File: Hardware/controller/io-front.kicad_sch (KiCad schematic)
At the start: 14 parts

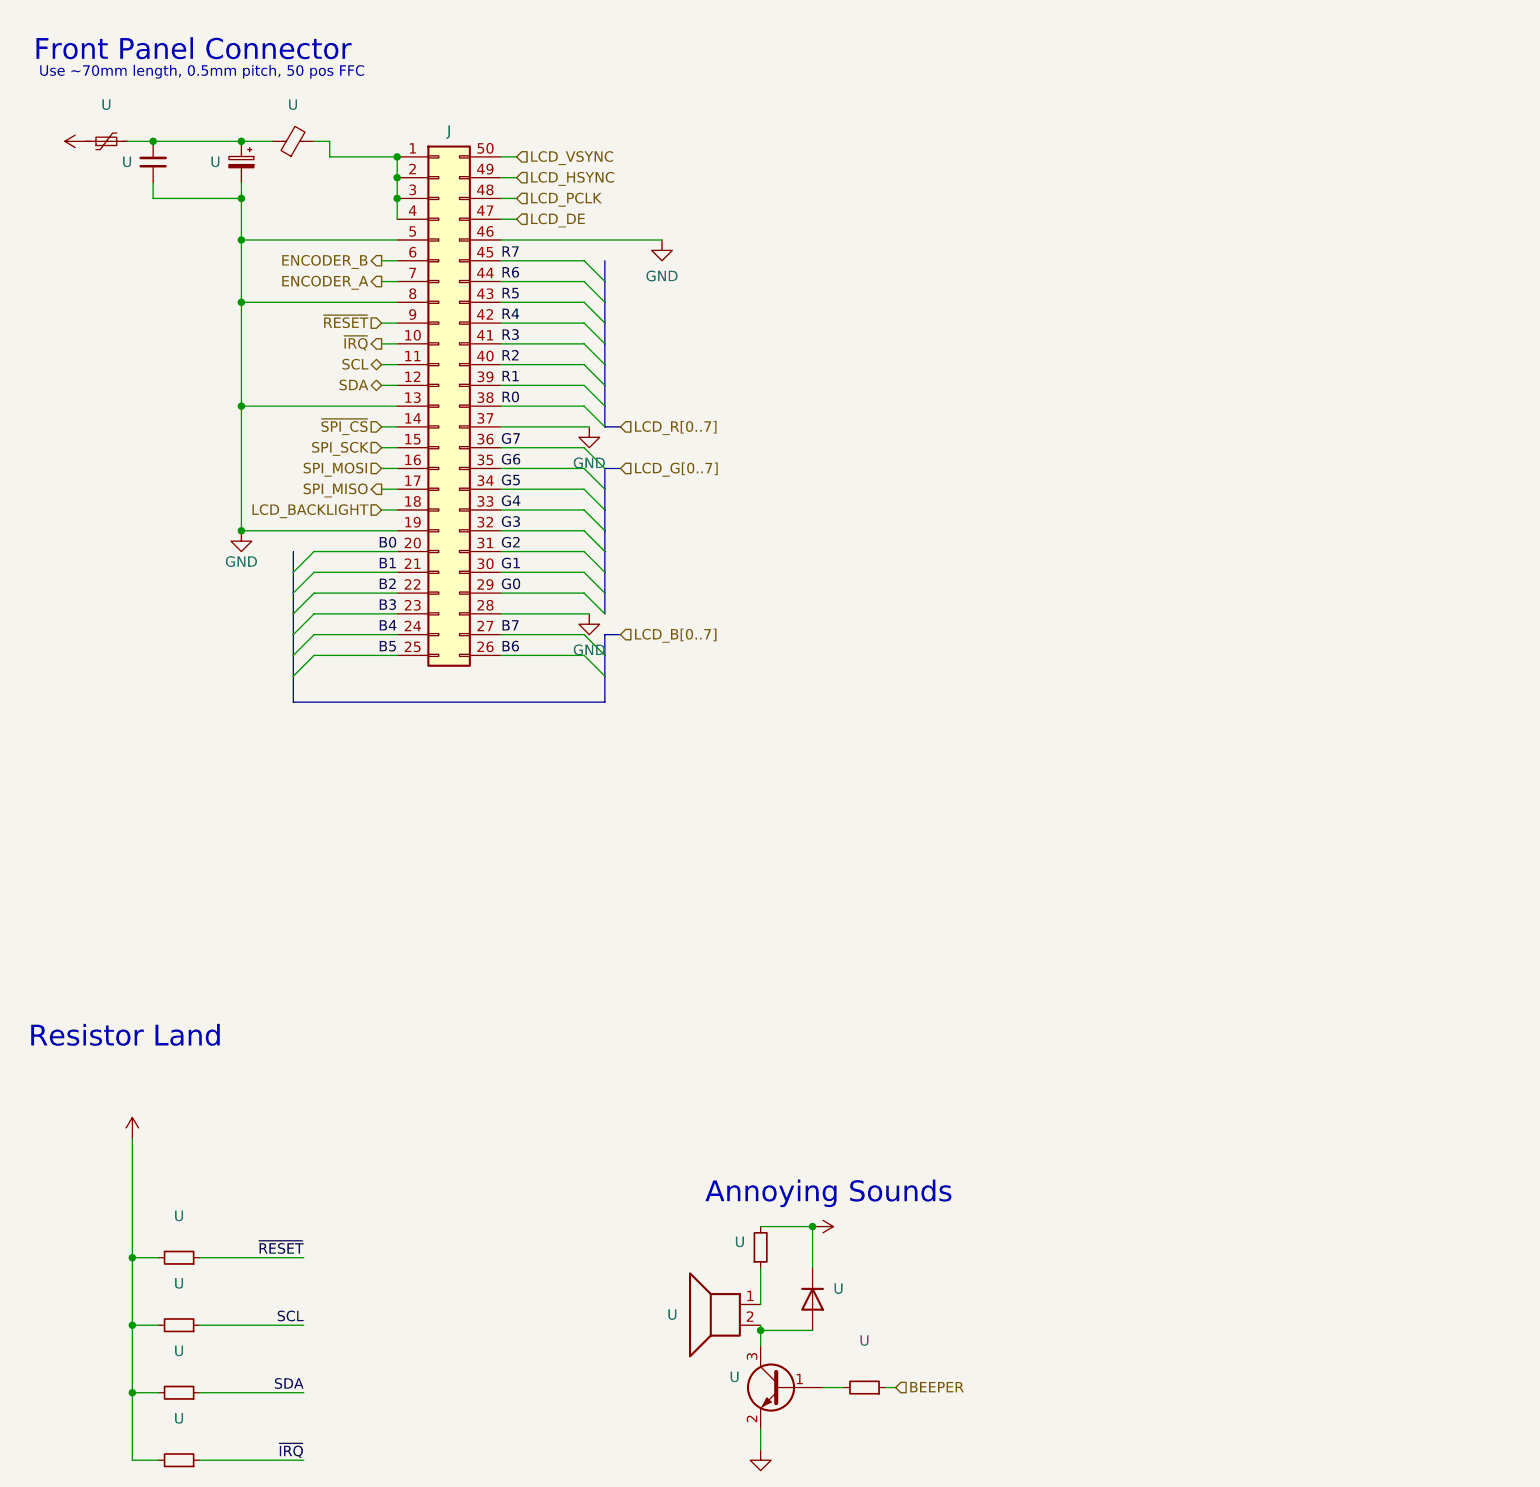
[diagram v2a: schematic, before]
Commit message: Route controller front panel connections
- Routed the connections to the front panel flex connector (the RGB
  interface, SPI + I2C, and various control signals and its fused power
  rail) and the SoM

- Tweaked SoM symbols and footprint

- Added symbols for 4x 2:1 analog switch (SN74CBTLV3257)
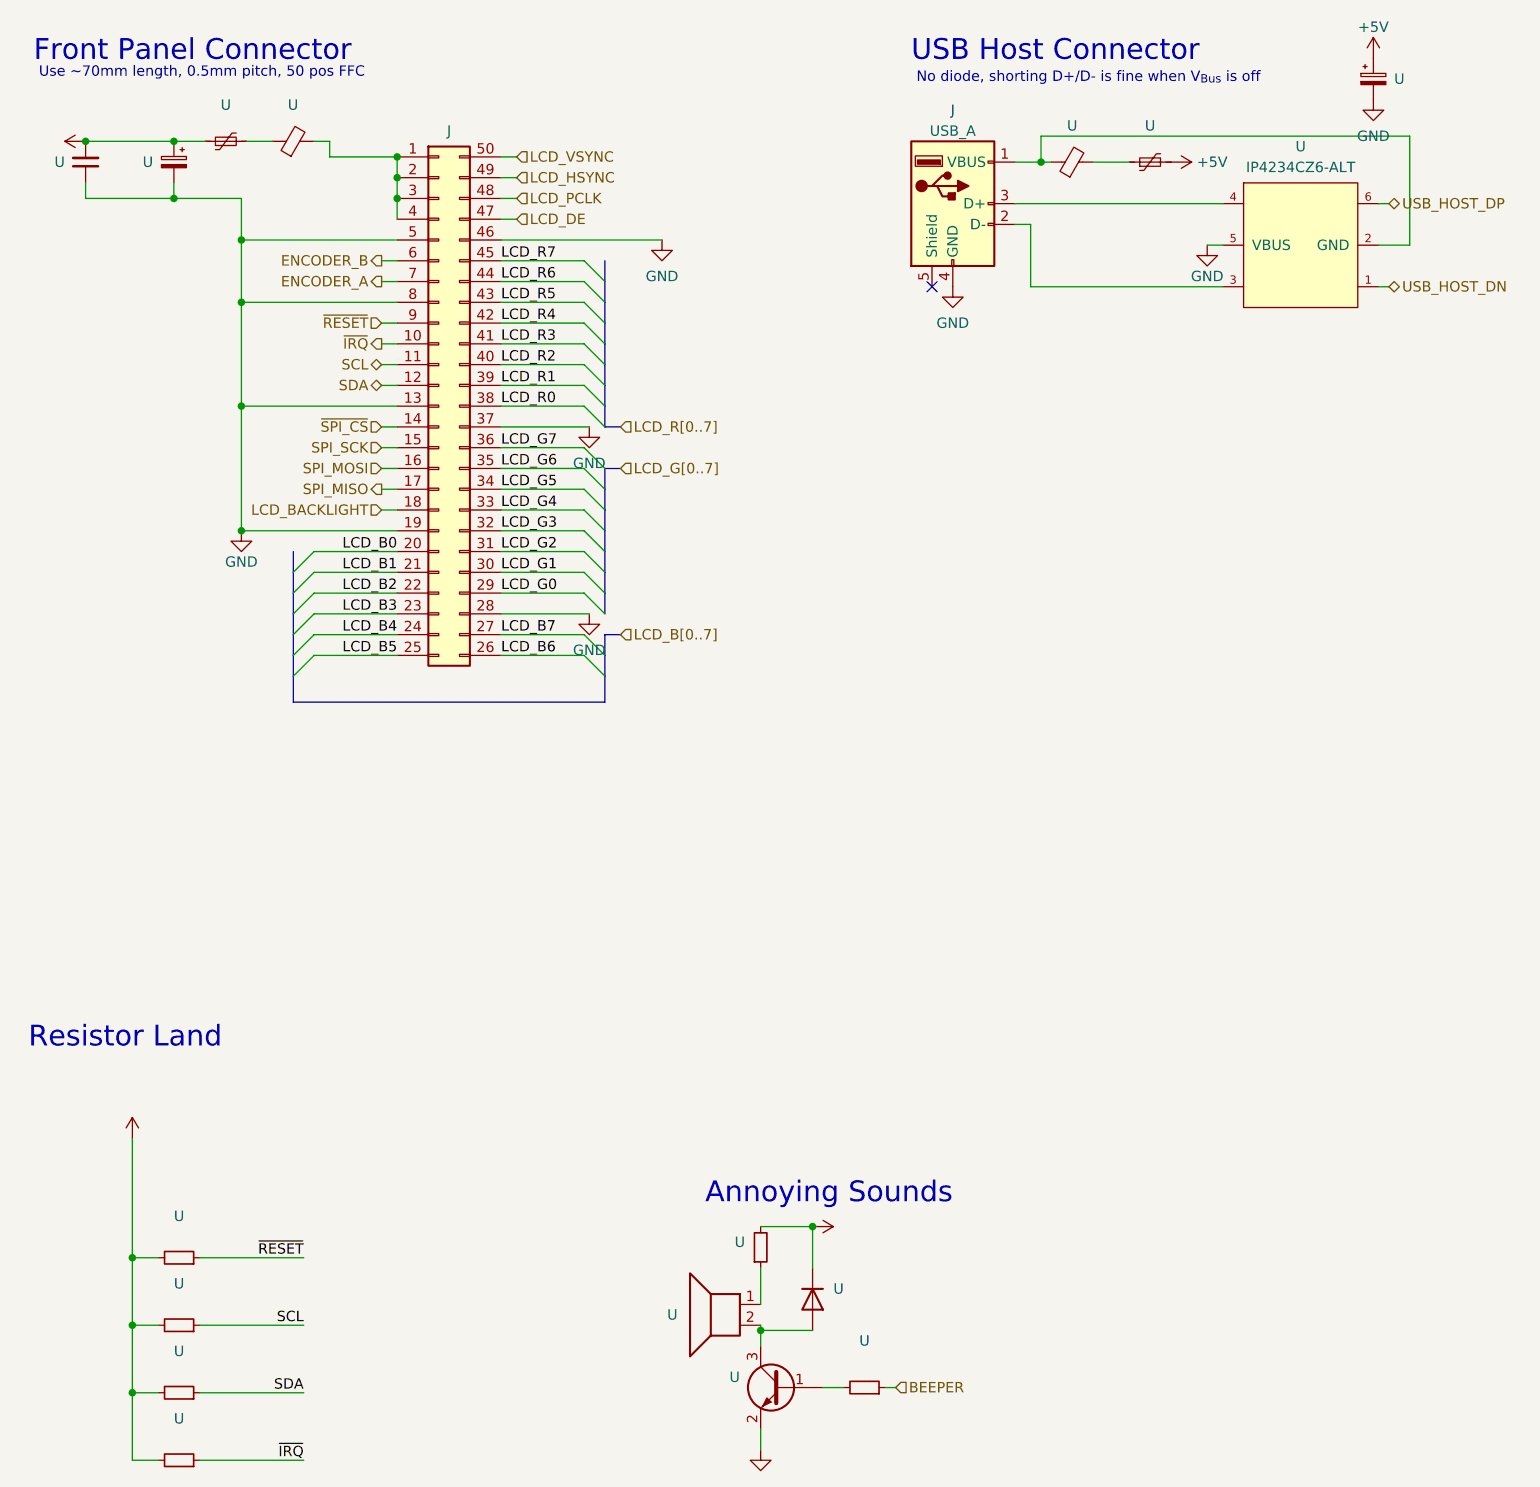
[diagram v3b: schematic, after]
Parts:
- added J: USB_A, symbol Connector:USB_A
- added U: (no value), symbol Device:Polyfuse_Small
- added U: (no value), symbol Device:FerriteBead_Small
- added U: IP4234CZ6-ALT, Package_SO:TSOP-6_1.65x3.05mm_P0.95mm, symbol programmable-load:IP4234CZ6-ALT
- added U: (no value), symbol Device:C_Polarized_Small
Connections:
- net +3V3: now also U.1, U.2
- net GND: now also J.4 (GND), U.2, U.5 (VBUS)
- net at U.1, U.2: no longer U.1, U.2
- net B0 renamed LCD_B0
- net B1 renamed LCD_B1
- net B2 renamed LCD_B2
- net B3 renamed LCD_B3
- net B4 renamed LCD_B4
- net B5 renamed LCD_B5
- net B6 renamed LCD_B6
- net B7 renamed LCD_B7
- net G0 renamed LCD_G0
- net G1 renamed LCD_G1
- net G2 renamed LCD_G2
- net G3 renamed LCD_G3
- net G4 renamed LCD_G4
- net G5 renamed LCD_G5
- net G6 renamed LCD_G6
- net G7 renamed LCD_G7
- net R0 renamed LCD_R0
- net R1 renamed LCD_R1
- net R2 renamed LCD_R2
- net R3 renamed LCD_R3
- net R4 renamed LCD_R4
- net R5 renamed LCD_R5
- net R6 renamed LCD_R6
- net R7 renamed LCD_R7
- new net: U.1, U.2
- new net: J.1 (VBUS), U.1, U.2 (GND)
- new net: J.2 (D-), U.3
- new net: J.3 (D+), U.4
- new net +5V: U.1, U.2
- new net USB_HOST_DN: U.1
- new net USB_HOST_DP: U.6
- no-connect marks 0 -> 1
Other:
- note added: "No diode, shorting D+/D- is fine when V_{Bus} is off"
- note added: "USB Host Connector"
- moved on the sheet: U

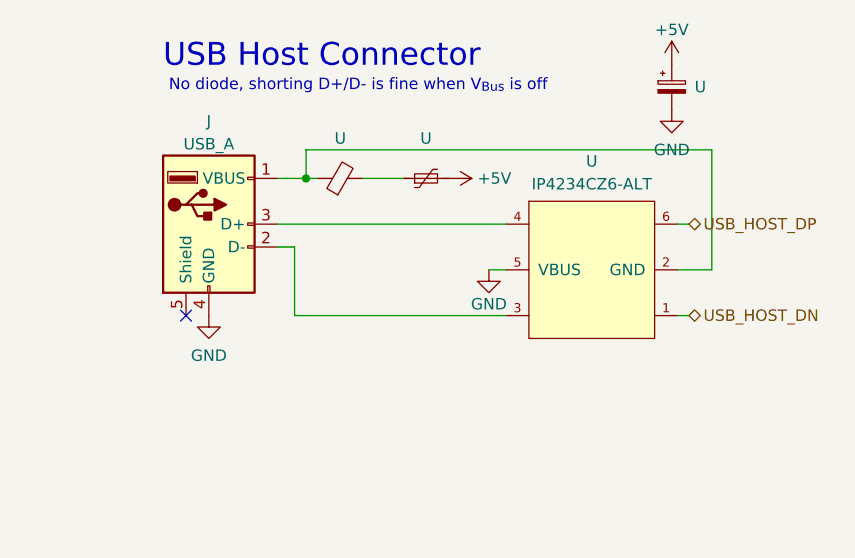
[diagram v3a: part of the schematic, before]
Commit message: More rework of controller
- Updated power section to use a transformer + DC/DC modules, rather
  than a switching AC/DC supply: this should result in fewer bits of
  random noise floating around

- Moved a bunch of stuff around, and changed pinouts slightly of
  external connectors

- Start work on removing dependency on rear IO board

- Minor tweaks to part numbers on front panel board
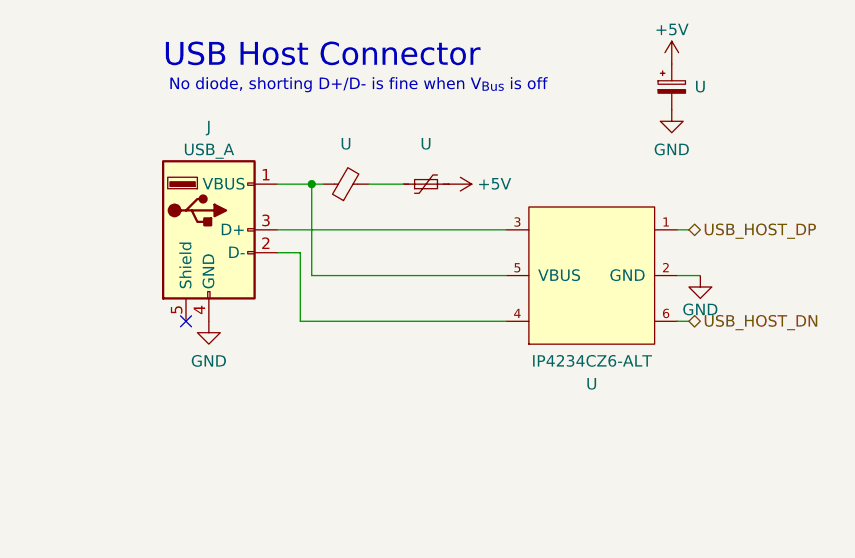
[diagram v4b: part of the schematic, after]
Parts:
- U: MPN EMVA250ADA470MF55G -> APA0606220M035R
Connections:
- net GND: now also U.2 (GND); no longer U.5 (VBUS)
- net USB_HOST_DN: now also U.6; no longer U.1
- net USB_HOST_DP: now also U.1; no longer U.6
- net at J.1 (VBUS), U.1: now also U.5 (VBUS); no longer U.2 (GND)
- net at J.2 (D-): now also U.4; no longer U.3
- net at J.3 (D+): now also U.3; no longer U.4
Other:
- moved on the sheet: J, U

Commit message: Replaced most passives with 0603 size
- This is more compact, and we might as well since this board will be at
  least partially assembled beforehand
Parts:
- U: MPN RMC1/10-103JTP -> (none)
- U: MPN RMC1/10-222JTP -> (none)
- U: MPN RMC1/10-331JTP -> (none)
- U: MPN CL21B104KACNFNC -> (none)
- U: MPn RMC1/10-331JTP -> (none)
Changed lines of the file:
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@@
       (effects (font (size 1.27 1.27)) hide)
     )
-    (property "MPN" "RMC1/10-103JTP" (id 4) (at 37.465 189.865 90)
+    (property "MPN" "" (id 4) (at 37.465 189.865 90)
       (effects (font (size 1.27 1.27)) hide)
     )
@@
       (effects (font (size 1.27 1.27)) hide)
     )
-    (property "MPN" "RMC1/10-103JTP" (id 4) (at 37.465 165.1 90)
+    (property "MPN" "" (id 4) (at 37.465 165.1 90)
       (effects (font (size 1.27 1.27)) hide)
     )
@@
       (effects (font (size 1.27 1.27)) hide)
     )
-    (property "MPN" "RMC1/10-222JTP" (id 4) (at 37.465 181.61 90)
+    (property "MPN" "" (id 4) (at 37.465 181.61 90)
       (effects (font (size 1.27 1.27)) hide)
     )
@@
       (effects (font (size 1.27 1.27)) hide)
     )
-    (property "MPN" "RMC1/10-222JTP" (id 4) (at 37.465 173.355 90)
+    (property "MPN" "" (id 4) (at 37.465 173.355 90)
       (effects (font (size 1.27 1.27)) hide)
     )
@@
       (effects (font (size 1.27 1.27)) hide)
     )
-    (property "MPN" "RMC1/10-331JTP" (id 4) (at 108.585 163.83 0)
+    (property "MPN" "" (id 4) (at 108.585 163.83 0)
       (effects (font (size 1.27 1.27)) hide)
     )
@@
       (effects (font (size 1.27 1.27)) hide)
     )
-    (property "MPN" "CL21B104KACNFNC" (id 4) (at 26.035 31.115 0)
+    (property "MPN" "" (id 4) (at 26.035 31.115 0)
       (effects (font (size 1.27 1.27)) hide)
     )
@@
       (effects (font (size 1.27 1.27)) hide)
     )
-    (property "MPn" "RMC1/10-331JTP" (id 4) (at 121.285 180.975 0)
-      (effects (font (size 1.27 1.27)) hide)
-    )
+    (property "MPn" "" (id 4) (at 121.285 180.975 0)
+      (effects (font (size 1.27 1.27)) hide)
+    )

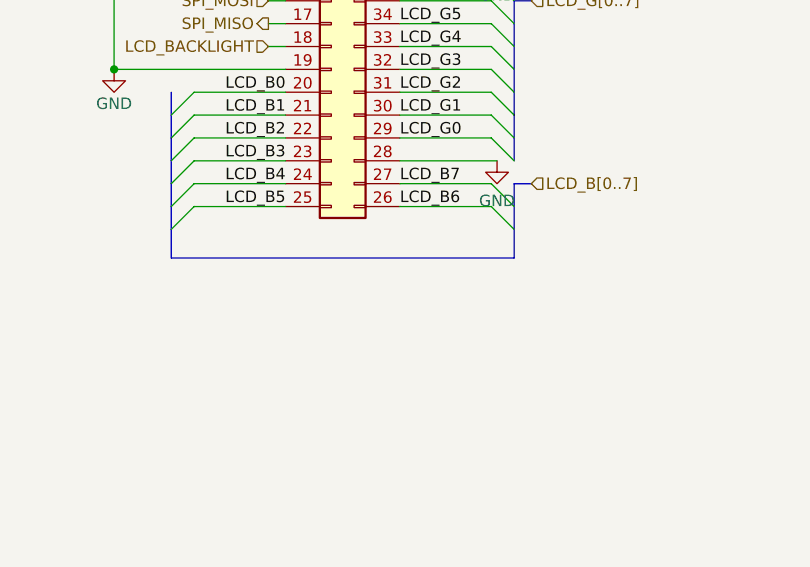
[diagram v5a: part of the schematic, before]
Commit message: Routed Ethernet PHY
- Finished routing the RMII lines to the Ethernet PHY, all of its power
  stuff, and routing its output signals to the Ethernet magjack on the
  side of the board

  This probably needs some revisiting re: the LAN8720 reference
  schematics and layouts
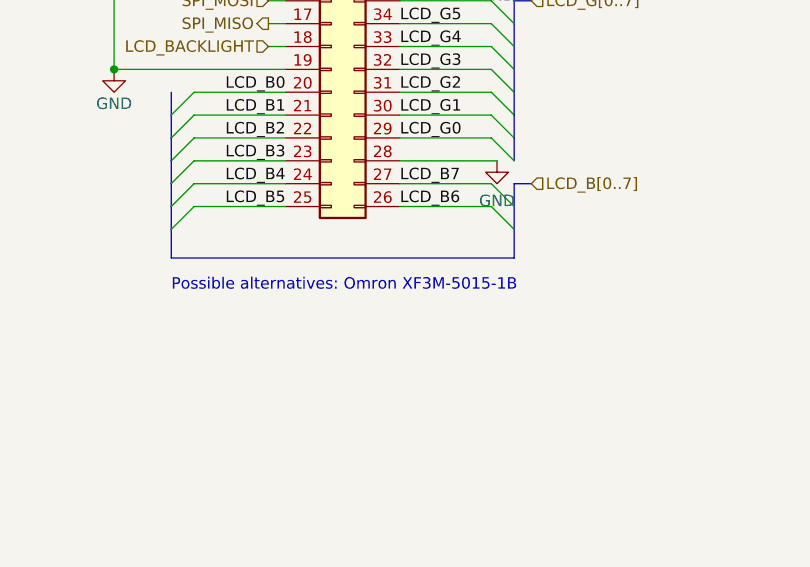
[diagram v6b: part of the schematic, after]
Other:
- note added: "Possible alternatives: Omron XF3M-5015-1B"
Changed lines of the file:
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@@
     (effects (font (size 2.54 2.54)) (justify left bottom))
+  )
+  (text "Possible alternatives: Omron XF3M-5015-1B" (at 51.435 100.965 0)
+    (effects (font (size 1.27 1.27)) (justify left bottom))
   )
   (text "USB Host Connector" (at 127 19.05 0)

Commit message: Auxiliary I2C + SPI bus routing
- Added an I2C MAC EEPROM to the aux I2C bus, which will be read for the
  device serial and Ethernet MAC address

- Add fan controller, filtering/ESD and fusing for expansion connector
  for rear IO section. We'll still have to add the CAN termination as
  well as the CAN transceiver on that part

- Minor routing + pin location tweaks
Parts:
- added U: (no value), symbol Device:R_Small
- U: MPN APA0606220M035R -> A768EB336M1GLAE045
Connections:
- net +3V3: now also U.2
- net ~{SPI_CS}: now also U.1
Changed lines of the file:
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@@
   (junction (at 64.135 35.56) (diameter 0) (color 0 0 0 0)
+  )
+  (junction (at 31.75 156.845) (diameter 0) (color 0 0 0 0)
   )
   (junction (at 36.83 35.56) (diameter 0) (color 0 0 0 0)
@@
     (stroke (width 0) (type default))
   )
+  (wire (pts (xy 40.005 156.845) (xy 52.705 156.845))
+    (stroke (width 0) (type default))
+  )
   (bus (pts (xy 89.535 63.5) (xy 91.44 63.5))
     (stroke (width 0) (type default))
@@
     (stroke (width 0) (type default))
   )
-  (wire (pts (xy 31.75 150.495) (xy 31.75 165.1))
+  (wire (pts (xy 31.75 150.495) (xy 31.75 156.845))
     (stroke (width 0) (type default))
   )
@@
     (stroke (width 0) (type default))
   )
+  (wire (pts (xy 31.75 156.845) (xy 31.75 165.1))
+    (stroke (width 0) (type default))
+  )
   (wire (pts (xy 36.83 35.56) (xy 45.085 35.56))
     (stroke (width 0) (type default))
@@
   )
   (wire (pts (xy 86.995 78.74) (xy 76.835 78.74))
+    (stroke (width 0) (type default))
+  )
+  (wire (pts (xy 31.75 156.845) (xy 34.925 156.845))
     (stroke (width 0) (type default))
   )
@@
   )
   (label "LCD_B0" (at 64.135 78.74 0) (fields_autoplaced)
+    (effects (font (size 1.27 1.27)) (justify right bottom))
+  )
+  (label "~{SPI_CS}" (at 52.705 156.845 0) (fields_autoplaced)
     (effects (font (size 1.27 1.27)) (justify right bottom))
   )
@@
     (pin "2")
   )
+  (symbol (lib_id "Device:R_Small") (at 37.465 156.845 270) (mirror x) (unit 1)
+    (in_bom yes) (on_board yes)
+    (default_instance (reference "U") (unit 1) (value "") (footprint ""))
+    (property "Reference" "U" (id 0) (at 37.465 151.765 90)
+      (effects (font (size 1.27 1.27)))
+    )
+    (property "Value" "" (id 1) (at 37.465 154.305 90)
+      (effects (font (size 1.27 1.27)))
+    )
+    (property "Footprint" "" (id 2) (at 37.465 156.845 0)
+      (effects (font (size 1.27 1.27)) hide)
+    )
+    (property "Datasheet" "~" (id 3) (at 37.465 156.845 0)
+      (effects (font (size 1.27 1.27)) hide)
+    )
+    (property "MPN" "" (id 4) (at 37.465 156.845 90)
+      (effects (font (size 1.27 1.27)) hide)
+    )
+    (pin "1")
+    (pin "2")
+  )
   (symbol (lib_id "power:GND") (at 183.515 23.495 0) (unit 1)
     (in_bom yes) (on_board yes)
@@
       (effects (font (size 1.27 1.27)) hide)
     )
-    (property "MPN" "APA0606220M035R" (id 4) (at 183.515 20.955 0)
-      (effects (font (size 1.27 1.27)) hide)
-    )
+    (property "MPN" "A768EB336M1GLAE045" (id 4) (at 183.515 20.955 0)
+      (effects (font (size 1.27 1.27)) hide)
+    )
